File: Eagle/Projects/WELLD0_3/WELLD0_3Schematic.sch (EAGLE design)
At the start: 1 part

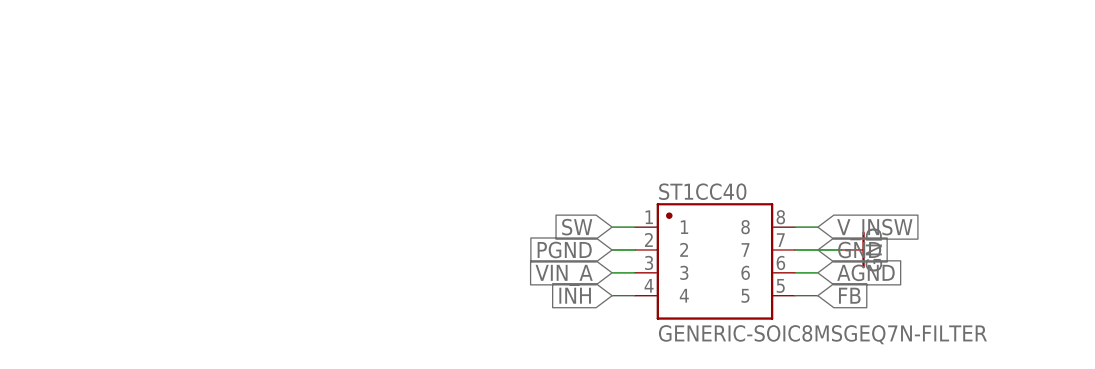
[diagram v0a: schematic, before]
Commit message: LED driver circuit made. (Almost) Have not considered supply, or turn off signal or the dimming mechanism
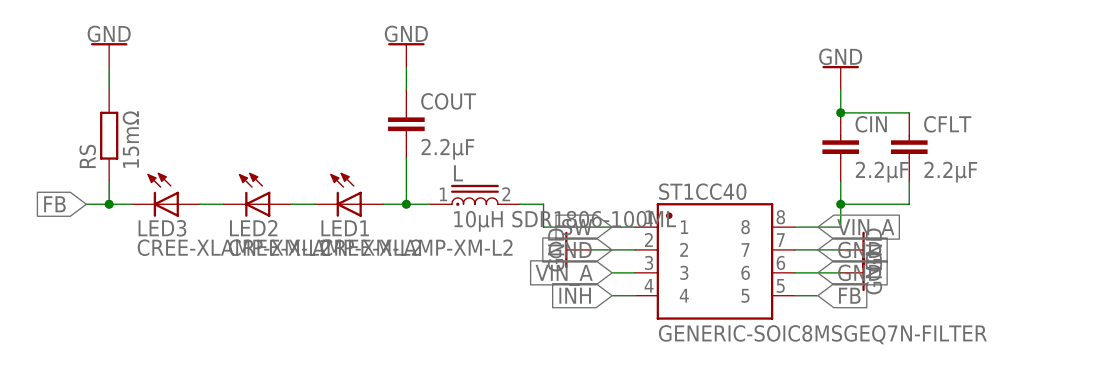
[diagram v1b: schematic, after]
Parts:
- added CFLT, CIN, COUT: 2.2µF, rcl:C-EUC0603
- added L: 10µH SDR1806-100ML, SDR1806-470ML:SDR1806-470ML
- added LED1, LED2, LED3: CREE-XLAMP-XM-L2, led:CREE-XLAMP-XM-L
- added RS: 15mΩ, rcl:R-EU_M1206
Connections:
- removed net AGND: ST1CC40.6
- removed net PGND: ST1CC40.2
- removed net V_INSW: ST1CC40.8
- new net N$1: COUT.2, L.1, LED1.A
- new net N$2: LED1.C, LED2.A
- new net N$3: LED2.C, LED3.A
- net FB: now also LED3.C, RS.1
- net GND: now also CFLT.1, CIN.1, COUT.1, RS.2, ST1CC40.2, ST1CC40.6
- net SW: now also L.2
- net VIN_A: now also CFLT.2, CIN.2, ST1CC40.8

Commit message: Work from 16/10-18
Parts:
- removed LED2: CREE-XLAMP-XM-L2, led:CREE-XLAMP-XM-L
- added J2: Battery, con-molex:22-27-2021-02
- added R1: 10K, audio amplifier example:R-US_R0603
- added RS1: 15mΩ, rcl:R-EU_M1206
- added S1: Switch, SparkFun-Switches:MOMENTARY-SWITCH-SPST-SMD-6.2MM-TALL
- added T1, T2: (no value), DC_LOAD_AU:-NPN-SOT23-BEC
- added U1: EFM8BB10F8G-µCBRZ, adg451_adg452_adg453:EFM8BB10F8G-µCBRZ
- added U2: CJT1117-3.3-SOT223, Seeed-IC:PMIC-CJT1117-3.3(SOT223)
- added X1: ProgramPins, con-molex:C-GRID-03-70543
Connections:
- removed net VIN_A: CFLT.2, CIN.2, ST1CC40.3, ST1CC40.8
- new net +7.4V: CFLT.2, CIN.2, J2-1.S, ST1CC40.3, ST1CC40.8, U2.IN
- new net C2D: U1.P2.0/C2D, X1-3.S
- new net DIM: T2.B, U1.P1.1
- new net RSTB/C2CI: U1.RSTB/C2CK, X1-2.S
- new net SWSIGN: R1.1, S1.1, U1.P0.5
- new net VDD: R1.2, U2.OUT
- net FB: now also RS1.1
- net GND: now also J2-2.S, S1.2, T2.E, U2.GND, X1-1.S
- net N$2: now also LED3.A; no longer LED2.A
- net N$3: now also RS1.2, T2.C; no longer LED2.C, LED3.A
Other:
- moved on the sheet: CFLT, CIN, ST1CC40

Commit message: Circuit done - i guess 24/10-18
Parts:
- removed R1: 10K, audio amplifier example:R-US_R0603
- removed S1: Switch, SparkFun-Switches:MOMENTARY-SWITCH-SPST-SMD-6.2MM-TALL
- removed T1: (no value), DC_LOAD_AU:-NPN-SOT23-BEC
- removed U1: EFM8BB10F8G-µCBRZ, adg451_adg452_adg453:EFM8BB10F8G-µCBRZ
- added ALT_USER_SW1, ALT_USER_SW2, ALT_USER_SW3, ALT_USER_SW4, LED+, LED-: (no value), SparkFun-Connectors:CONN_01
- added BOOTLOADER, RST_SW, USER_SW, USER_SW_ALT: Switch, SparkFun-Switches:MOMENTARY-SWITCH-SPST-SMD-6.2MM-TALL
- added C1, C2: 100nF, rcl:C-EUC0603
- added IC1: STM32F030F4P6TR, SamacSys_Parts:STM32F030F4P6TR
- added R2, R4: 10k, audio amplifier example:R-US_R0603
- added R3, R6: 10K, audio amplifier example:R-US_R0603
- added R5: R>12.5k, audio amplifier example:R-US_R0603
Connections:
- removed net C2D: U1.P2.0/C2D, X1-3.S
- removed net RSTB/C2CI: U1.RSTB/C2CK, X1-2.S
- removed net SWSIGN: R1.1, S1.1, U1.P0.5
- removed net VDD: R1.2, U2.OUT
- new net +3.3V: BOOTLOADER.1, IC1.VDD, IC1.VDDA, R3.2, R6.2, U2.OUT
- new net ADC_BATTERY: IC1.PA0, R4.2, R5.1
- new net N$4: ALT_USER_SW3.1, USER_SW_ALT.1
- new net N$5: ALT_USER_SW4.1, USER_SW_ALT.2
- new net N$6: IC1.BOOT0, R2.1
- new net NRST: C1.1, IC1.NRST, R6.1, RST_SW.2
- new net SWSIGN1: ALT_USER_SW1.1, C2.1, IC1.PA7, R3.1, USER_SW.1
- new net UART_RX: IC1.PA10, X1-2.S
- new net UART_TX: IC1.PA9, X1-3.S
- net +7.4V: now also R5.2
- net DIM: now also IC1.PA6; no longer U1.P1.1
- net FB: now also LED-.1
- net GND: now also ALT_USER_SW2.1, BOOTLOADER.2, C1.2, C2.2, IC1.VSS, R2.2, R4.1, RST_SW.1, USER_SW.2; no longer S1.2
- net INH: now also IC1.PA5
- net N$1: now also LED+.1
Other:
- moved on the sheet: CFLT, CIN, COUT, L, LED1, LED3, RS, RS1, ST1CC40, T2, U2

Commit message: Ready for final thoughts
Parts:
- removed X1: ProgramPins, con-molex:C-GRID-03-70543
- added PROGRAMPINS: (no value), con-lstb:MA04-1
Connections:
- net +7.4V: now also PROGRAMPINS.4
- net GND: now also PROGRAMPINS.3; no longer X1-1.S
- net SWSIGN1: now also IC1.PA2; no longer IC1.PA7
- net UART_RX: now also PROGRAMPINS.1; no longer X1-2.S
- net UART_TX: now also PROGRAMPINS.2; no longer X1-3.S
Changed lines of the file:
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@@
 <part name="J2" library="con-molex" library_urn="urn:adsk.eagle:library:165" deviceset="22-?-02" device="27-2021" value="Battery"/>
 <part name="RS1" library="rcl" library_urn="urn:adsk.eagle:library:334" deviceset="R-EU_" device="M1206" package3d_urn="urn:adsk.eagle:package:23566/1" value="15mΩ"/>
-<part name="X1" library="con-molex" library_urn="urn:adsk.eagle:library:165" deviceset="C-GRID-03" device="-70543" value="ProgramPins"/>
 <part name="IC1" library="SamacSys_Parts" deviceset="STM32F030F4P6TR" device=""/>
 <part name="GND8" library="SparkFun-PowerSymbols" library_urn="urn:adsk.eagle:library:530" deviceset="GND" device=""/>
@@
 <part name="ALT_USER_SW4" library="SparkFun-Connectors" library_urn="urn:adsk.eagle:library:513" deviceset="CONN_01" device="" package3d_urn="urn:adsk.eagle:package:38028/1"/>
 <part name="USER_SW_ALT" library="SparkFun-Switches" library_urn="urn:adsk.eagle:library:535" deviceset="MOMENTARY-SWITCH-SPST" device="-SMD-6.2MM-TALL" package3d_urn="urn:adsk.eagle:package:40172/1" value="Switch"/>
+<part name="PROGRAMPINS" library="con-lstb" library_urn="urn:adsk.eagle:library:162" deviceset="MA04-1" device="" package3d_urn="urn:adsk.eagle:package:8337/1"/>
 </parts>
 <sheets>
@@
 <attribute name="VALUE" x="56.642" y="90.17" size="1.778" layer="96" rot="R90"/>
 </instance>
-<instance part="X1" gate="-1" x="-81.28" y="33.02">
-<attribute name="NAME" x="-78.74" y="32.258" size="1.524" layer="95"/>
-<attribute name="VALUE" x="-82.042" y="34.417" size="1.778" layer="96"/>
-</instance>
-<instance part="X1" gate="-2" x="-81.28" y="30.48">
-<attribute name="NAME" x="-78.74" y="29.718" size="1.524" layer="95"/>
-</instance>
-<instance part="X1" gate="-3" x="-81.28" y="27.94">
-<attribute name="NAME" x="-78.74" y="27.178" size="1.524" layer="95"/>
-</instance>
 <instance part="IC1" gate="G$1" x="-30.48" y="17.78">
 <attribute name="NAME" x="3.81" y="25.4" size="1.778" layer="95" align="center-left"/>
@@
 <attribute name="NAME" x="114.3" y="-13.716" size="1.778" layer="95" font="vector" align="bottom-center"/>
 <attribute name="VALUE" x="114.3" y="-15.748" size="1.778" layer="96" font="vector" align="top-center"/>
+</instance>
+<instance part="PROGRAMPINS" gate="1" x="-99.06" y="-2.54">
+<attribute name="VALUE" x="-100.33" y="-12.7" size="1.778" layer="96"/>
+<attribute name="NAME" x="-100.33" y="3.302" size="1.778" layer="95"/>
 </instance>
 </instances>
@@
 <wire x1="81.28" y1="27.94" x2="81.28" y2="25.4" width="0.1524" layer="91"/>
 <label x="81.28" y="25.4" size="1.778" layer="95" rot="R270" xref="yes"/>
-</segment>
-<segment>
-<pinref part="X1" gate="-1" pin="S"/>
-<wire x1="-83.82" y1="33.02" x2="-86.36" y2="33.02" width="0.1524" layer="91"/>
-<label x="-86.36" y="33.02" size="1.778" layer="95" rot="R180" xref="yes"/>
 </segment>
 <segment>
@@
 <wire x1="-43.18" y1="22.86" x2="-43.18" y2="17.78" width="0.1524" layer="91"/>
 <junction x="-43.18" y="17.78"/>
+</segment>
+<segment>
+<pinref part="PROGRAMPINS" gate="1" pin="3"/>
+<wire x1="-91.44" y1="-2.54" x2="-88.9" y2="-2.54" width="0.1524" layer="91"/>
+<label x="-88.9" y="-2.54" size="1.778" layer="95" xref="yes"/>
 </segment>
 </net>
@@
 <label x="-76.2" y="17.78" size="1.778" layer="95" rot="R180" xref="yes"/>
 </segment>
+<segment>
+<pinref part="PROGRAMPINS" gate="1" pin="4"/>
+<wire x1="-91.44" y1="0" x2="-88.9" y2="0" width="0.1524" layer="91"/>
+<label x="-88.9" y="0" size="1.778" layer="95" xref="yes"/>
+</segment>
 </net>
 <net name="+3.3V" class="0">
@@
 </segment>
 <segment>
-<pinref part="X1" gate="-3" pin="S"/>
-<wire x1="-83.82" y1="27.94" x2="-86.36" y2="27.94" width="0.1524" layer="91"/>
-<label x="-86.36" y="27.94" size="1.778" layer="95" rot="R180" xref="yes"/>
+<pinref part="PROGRAMPINS" gate="1" pin="2"/>
+<wire x1="-91.44" y1="-5.08" x2="-88.9" y2="-5.08" width="0.1524" layer="91"/>
+<label x="-88.9" y="-5.08" size="1.778" layer="95" xref="yes"/>
 </segment>
 </net>
@@
 </segment>
 <segment>
-<pinref part="X1" gate="-2" pin="S"/>
-<wire x1="-83.82" y1="30.48" x2="-86.36" y2="30.48" width="0.1524" layer="91"/>
-<label x="-86.36" y="30.48" size="1.778" layer="95" rot="R180" xref="yes"/>
+<pinref part="PROGRAMPINS" gate="1" pin="1"/>
+<wire x1="-91.44" y1="-7.62" x2="-88.9" y2="-7.62" width="0.1524" layer="91"/>
+<label x="-88.9" y="-7.62" size="1.778" layer="95" xref="yes"/>
 </segment>
 </net>
 <net name="SWSIGN1" class="0">
 <segment>
-<pinref part="IC1" gate="G$1" pin="PA7"/>
-<label x="10.16" y="0" size="1.778" layer="95" xref="yes"/>
+<label x="45.72" y="0" size="1.778" layer="95" rot="R180" xref="yes"/>
 <pinref part="USER_SW" gate="G$1" pin="1"/>
 <wire x1="55.88" y1="0" x2="53.34" y2="0" width="0.1524" layer="91"/>
 <pinref part="R3" gate="G$1" pin="1"/>
 <wire x1="53.34" y1="0" x2="45.72" y2="0" width="0.1524" layer="91"/>
-<wire x1="45.72" y1="0" x2="7.62" y2="0" width="0.1524" layer="91"/>
 <wire x1="45.72" y1="5.08" x2="45.72" y2="0" width="0.1524" layer="91"/>
-<junction x="45.72" y="0"/>
 <pinref part="C2" gate="G$1" pin="1"/>
 <wire x1="53.34" y1="0" x2="53.34" y2="-10.16" width="0.1524" layer="91"/>
@@
 <junction x="53.34" y="-10.16"/>
 </segment>
-</net>
+<segment>
+<pinref part="IC1" gate="G$1" pin="PA2"/>
+<wire x1="-30.48" y1="0" x2="-33.02" y2="0" width="0.1524" layer="91"/>
+<label x="-33.02" y="0" size="1.778" layer="95" rot="R180" xref="yes"/>
+</segment>
+</net>

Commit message: Final form - missing heatsink
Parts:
- removed BOOTLOADER: Switch, SparkFun-Switches:MOMENTARY-SWITCH-SPST-SMD-6.2MM-TALL
- removed PROGRAMPINS: (no value), con-lstb:MA04-1
- added C3: 2.2µF, rcl:C-EUC0603
- added SV1: (no value), con-lstb:MA06-1
- BAT+: value Battery -> BAT-
- renumbered J2 to BAT+
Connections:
- new net BOOTJUMP: R2.2, SV1.5
- net +3.3V: now also C3.1, SV1.6, U2.IN; no longer BOOTLOADER.1, U2.OUT
- net +7.4V: now also SV1.3, U2.GND; no longer PROGRAMPINS.4, U2.IN
- net GND: now also C3.2, SV1.4, U2.OUT; no longer BOOTLOADER.2, PROGRAMPINS.3, R2.2, U2.GND
- net UART_RX: now also SV1.1; no longer PROGRAMPINS.1
- net UART_TX: now also SV1.2; no longer PROGRAMPINS.2

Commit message: Ordered PCB
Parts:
- removed LED1, LED3: CREE-XLAMP-XM-L2, led:CREE-XLAMP-XM-L
- added LED2, LED4: CREE-XLAMP-XM-L, led1:CREE-XLAMP-XM-L
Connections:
- net FB: now also LED2.C; no longer LED3.C
- net GND: now also LED2.HEATSINK, LED4.HEATSINK
- net N$1: now also LED4.A; no longer LED1.A
- net N$2: now also LED2.A, LED4.C; no longer LED1.C, LED3.A
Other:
- moved on the sheet: RS, RS1, T2
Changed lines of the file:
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@@
 <part name="ST1CC40" library="SparkFun-Retired" deviceset="GENERIC-SOIC8" device="MSGEQ7N-FILTER"/>
 <part name="GND1" library="SparkFun-PowerSymbols" library_urn="urn:adsk.eagle:library:530" deviceset="GND" device=""/>
-<part name="LED1" library="led" library_urn="urn:adsk.eagle:library:259" deviceset="CREE-XLAMP-XM-L" device="" package3d_urn="urn:adsk.eagle:package:15887/1" value="CREE-XLAMP-XM-L2"/>
-<part name="LED3" library="led" library_urn="urn:adsk.eagle:library:259" deviceset="CREE-XLAMP-XM-L" device="" package3d_urn="urn:adsk.eagle:package:15887/1" value="CREE-XLAMP-XM-L2"/>
 <part name="L" library="SDR1806-470ML" deviceset="SDR1806-470ML" device="" value="10µH SDR1806-100ML"/>
 <part name="COUT" library="rcl" library_urn="urn:adsk.eagle:library:334" deviceset="C-EU" device="C0603" package3d_urn="urn:adsk.eagle:package:23616/2" value="2.2µF"/>
@@
 <part name="GND7" library="SparkFun-PowerSymbols" library_urn="urn:adsk.eagle:library:530" deviceset="GND" device=""/>
 <part name="SV1" library="con-lstb" library_urn="urn:adsk.eagle:library:162" deviceset="MA06-1" device="" package3d_urn="urn:adsk.eagle:package:8340/1"/>
+<part name="LED2" library="led1" deviceset="CREE-XLAMP-XM-L" device="" package3d_urn="urn:adsk.eagle:package:15887/1"/>
+<part name="LED4" library="led1" deviceset="CREE-XLAMP-XM-L" device="" package3d_urn="urn:adsk.eagle:package:15887/1"/>
+<part name="GND11" library="SparkFun-PowerSymbols" library_urn="urn:adsk.eagle:library:530" deviceset="GND" device=""/>
+<part name="GND13" library="SparkFun-PowerSymbols" library_urn="urn:adsk.eagle:library:530" deviceset="GND" device=""/>
 </parts>
 <sheets>
@@
 <attribute name="VALUE" x="150.114" y="81.28" size="1.778" layer="96" rot="R90" align="top-center"/>
 </instance>
-<instance part="LED1" gate="G$1" x="73.66" y="86.36" rot="R270">
-<attribute name="NAME" x="69.088" y="82.804" size="1.778" layer="95"/>
-<attribute name="VALUE" x="69.088" y="80.645" size="1.778" layer="96"/>
-</instance>
-<instance part="LED3" gate="G$1" x="53.34" y="86.36" rot="R270">
-<attribute name="NAME" x="48.768" y="82.804" size="1.778" layer="95"/>
-<attribute name="VALUE" x="48.768" y="80.645" size="1.778" layer="96"/>
-</instance>
 <instance part="L" gate="G$1" x="86.36" y="86.36">
 <attribute name="NAME" x="83.812790625" y="88.907209375" size="1.78305" layer="95"/>
@@
 <attribute name="VALUE" x="80.264" y="91.821" size="1.778" layer="96"/>
 </instance>
-<instance part="RS" gate="G$1" x="45.72" y="93.98" rot="R90">
-<attribute name="NAME" x="44.2214" y="90.17" size="1.778" layer="95" rot="R90"/>
-<attribute name="VALUE" x="49.022" y="90.17" size="1.778" layer="96" rot="R90"/>
-</instance>
-<instance part="GND2" gate="1" x="50.8" y="116.84" rot="R180">
-<attribute name="VALUE" x="50.8" y="117.094" size="1.778" layer="96" rot="R180" align="top-center"/>
+<instance part="RS" gate="G$1" x="45.72" y="99.06" rot="R90">
+<attribute name="NAME" x="44.2214" y="95.25" size="1.778" layer="95" rot="R90"/>
+<attribute name="VALUE" x="49.022" y="95.25" size="1.778" layer="96" rot="R90"/>
+</instance>
+<instance part="GND2" gate="1" x="50.8" y="121.92" rot="R180">
+<attribute name="VALUE" x="50.8" y="122.174" size="1.778" layer="96" rot="R180" align="top-center"/>
 </instance>
 <instance part="GND3" gate="1" x="78.74" y="104.14" rot="R180">
@@
 <attribute name="VALUE" x="81.28" y="39.37" size="1.27" layer="96"/>
 </instance>
-<instance part="T2" gate="G$1" x="55.88" y="106.68" rot="R180">
-<attribute name="NAME" x="66.04" y="99.06" size="1.778" layer="95" rot="R180"/>
-<attribute name="VALUE" x="66.04" y="101.6" size="1.778" layer="96" rot="R180"/>
+<instance part="T2" gate="G$1" x="55.88" y="111.76" rot="R180">
+<attribute name="NAME" x="66.04" y="104.14" size="1.778" layer="95" rot="R180"/>
+<attribute name="VALUE" x="66.04" y="106.68" size="1.778" layer="96" rot="R180"/>
 </instance>
 <instance part="BAT+" gate="-1" x="-71.12" y="58.42">
@@
 <attribute name="NAME" x="-68.58" y="52.578" size="1.524" layer="95"/>
 </instance>
-<instance part="RS1" gate="G$1" x="53.34" y="93.98" rot="R90">
-<attribute name="NAME" x="51.8414" y="90.17" size="1.778" layer="95" rot="R90"/>
-<attribute name="VALUE" x="56.642" y="90.17" size="1.778" layer="96" rot="R90"/>
+<instance part="RS1" gate="G$1" x="53.34" y="99.06" rot="R90">
+<attribute name="NAME" x="51.8414" y="95.25" size="1.778" layer="95" rot="R90"/>
+<attribute name="VALUE" x="56.642" y="95.25" size="1.778" layer="96" rot="R90"/>
 </instance>
 <instance part="IC1" gate="G$1" x="-30.48" y="17.78">
@@
 <attribute name="VALUE" x="-102.87" y="-12.7" size="1.778" layer="96"/>
 <attribute name="NAME" x="-102.87" y="8.382" size="1.778" layer="95"/>
+</instance>
+<instance part="LED2" gate="G$1" x="53.34" y="81.28" rot="R270">
+<attribute name="NAME" x="48.768" y="77.724" size="1.778" layer="95"/>
+<attribute name="VALUE" x="48.768" y="75.565" size="1.778" layer="96"/>
+</instance>
+<instance part="LED4" gate="G$1" x="73.66" y="81.28" rot="R270">
+<attribute name="NAME" x="69.088" y="77.724" size="1.778" layer="95"/>
+<attribute name="VALUE" x="69.088" y="75.565" size="1.778" layer="96"/>
+</instance>
+<instance part="GND11" gate="1" x="50.8" y="91.44" rot="R180">
+<attribute name="VALUE" x="50.8" y="91.694" size="1.778" layer="96" rot="R180" align="top-center"/>
+</instance>
+<instance part="GND13" gate="1" x="71.12" y="91.44" rot="R180">
+<attribute name="VALUE" x="71.12" y="91.694" size="1.778" layer="96" rot="R180" align="top-center"/>
 </instance>
 </instances>
@@
 <pinref part="T2" gate="G$1" pin="E"/>
 <pinref part="GND2" gate="1" pin="GND"/>
-<wire x1="53.34" y1="111.76" x2="53.34" y2="114.3" width="0.1524" layer="91"/>
-<wire x1="53.34" y1="114.3" x2="50.8" y2="114.3" width="0.1524" layer="91"/>
+<wire x1="53.34" y1="116.84" x2="53.34" y2="119.38" width="0.1524" layer="91"/>
+<wire x1="53.34" y1="119.38" x2="50.8" y2="119.38" width="0.1524" layer="91"/>
 <pinref part="RS" gate="G$1" pin="2"/>
-<wire x1="45.72" y1="99.06" x2="45.72" y2="114.3" width="0.1524" layer="91"/>
-<wire x1="45.72" y1="114.3" x2="50.8" y2="114.3" width="0.1524" layer="91"/>
-<junction x="50.8" y="114.3"/>
+<wire x1="45.72" y1="104.14" x2="45.72" y2="119.38" width="0.1524" layer="91"/>
+<wire x1="45.72" y1="119.38" x2="50.8" y2="119.38" width="0.1524" layer="91"/>
+<junction x="50.8" y="119.38"/>
 </segment>
 <segment>
@@
 <label x="96.52" y="35.56" size="1.778" layer="95" xref="yes"/>
 </segment>
+<segment>
+<pinref part="GND11" gate="1" pin="GND"/>
+<pinref part="LED2" gate="G$1" pin="HEATSINK"/>
+<wire x1="50.8" y1="88.9" x2="50.8" y2="86.36" width="0.1524" layer="91"/>
+</segment>
+<segment>
+<pinref part="GND13" gate="1" pin="GND"/>
+<pinref part="LED4" gate="G$1" pin="HEATSINK"/>
+<wire x1="71.12" y1="88.9" x2="71.12" y2="86.36" width="0.1524" layer="91"/>
+</segment>
 </net>
 <net name="FB" class="0">
@@
 </segment>
 <segment>
-<pinref part="LED3" gate="G$1" pin="C"/>
 <label x="43.18" y="86.36" size="1.778" layer="95" rot="R180" xref="yes"/>
 <wire x1="48.26" y1="86.36" x2="45.72" y2="86.36" width="0.1524" layer="91"/>
 <pinref part="RS" gate="G$1" pin="1"/>
 <wire x1="45.72" y1="86.36" x2="43.18" y2="86.36" width="0.1524" layer="91"/>
-<wire x1="45.72" y1="88.9" x2="45.72" y2="86.36" width="0.1524" layer="91"/>
+<wire x1="45.72" y1="93.98" x2="45.72" y2="86.36" width="0.1524" layer="91"/>
 <junction x="45.72" y="86.36"/>
 <pinref part="RS1" gate="G$1" pin="1"/>
-<wire x1="53.34" y1="88.9" x2="45.72" y2="88.9" width="0.1524" layer="91"/>
-<junction x="45.72" y="88.9"/>
+<wire x1="53.34" y1="93.98" x2="45.72" y2="93.98" width="0.1524" layer="91"/>
+<junction x="45.72" y="93.98"/>
 <pinref part="LED-" gate="G$1" pin="1"/>
 <wire x1="45.72" y1="86.36" x2="45.72" y2="78.74" width="0.1524" layer="91"/>
+<pinref part="LED2" gate="G$1" pin="C"/>
+<wire x1="48.26" y1="86.36" x2="48.26" y2="81.28" width="0.1524" layer="91"/>
 </segment>
 </net>
@@
 <segment>
 <pinref part="L" gate="G$1" pin="1"/>
-<pinref part="LED1" gate="G$1" pin="A"/>
 <wire x1="81.28" y1="86.36" x2="78.74" y2="86.36" width="0.1524" layer="91"/>
 <pinref part="COUT" gate="G$1" pin="2"/>
@@
 <pinref part="LED+" gate="G$1" pin="1"/>
 <wire x1="78.74" y1="86.36" x2="78.74" y2="78.74" width="0.1524" layer="91"/>
+<pinref part="LED4" gate="G$1" pin="A"/>
+<wire x1="76.2" y1="81.28" x2="76.2" y2="86.36" width="0.1524" layer="91"/>
 </segment>
 </net>
 <net name="N$2" class="0">
 <segment>
-<pinref part="LED1" gate="G$1" pin="C"/>
-<pinref part="LED3" gate="G$1" pin="A"/>
 <wire x1="68.58" y1="86.36" x2="55.88" y2="86.36" width="0.1524" layer="91"/>
+<pinref part="LED2" gate="G$1" pin="A"/>
+<wire x1="55.88" y1="86.36" x2="55.88" y2="81.28" width="0.1524" layer="91"/>
+<pinref part="LED4" gate="G$1" pin="C"/>
+<wire x1="68.58" y1="86.36" x2="68.58" y2="81.28" width="0.1524" layer="91"/>
 </segment>
 </net>
@@
 <pinref part="RS1" gate="G$1" pin="2"/>
 <pinref part="T2" gate="G$1" pin="C"/>
-<wire x1="53.34" y1="99.06" x2="53.34" y2="101.6" width="0.1524" layer="91"/>
+<wire x1="53.34" y1="104.14" x2="53.34" y2="106.68" width="0.1524" layer="91"/>
 </segment>
 </net>
@@
 <segment>
 <pinref part="T2" gate="G$1" pin="B"/>
-<wire x1="58.42" y1="106.68" x2="60.96" y2="106.68" width="0.1524" layer="91"/>
-<label x="60.96" y="106.68" size="1.778" layer="95" xref="yes"/>
-</segment>
-<segment>
+<wire x1="58.42" y1="111.76" x2="60.96" y2="111.76" width="0.1524" layer="91"/>
+<label x="60.96" y="111.76" size="1.778" layer="95" xref="yes"/>
+</segment>
+<segment>
